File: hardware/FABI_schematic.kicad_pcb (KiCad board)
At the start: 2 copper layers, 81 x 55 mm, 74 parts, among them J1 Conn_01x02_Pin, J11 009159005551906, J11_GND1 Conn_01x01_Male, J11_VDD1 Conn_01x01_Male, J11_data1 Conn_01x01_Male, J12 Conn_01x04_Socket, J2 display_connector_91601-304LF, J3 54601-906WPLF, J4 54-00174 / FC68125, J5 54-00174 / FC68125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

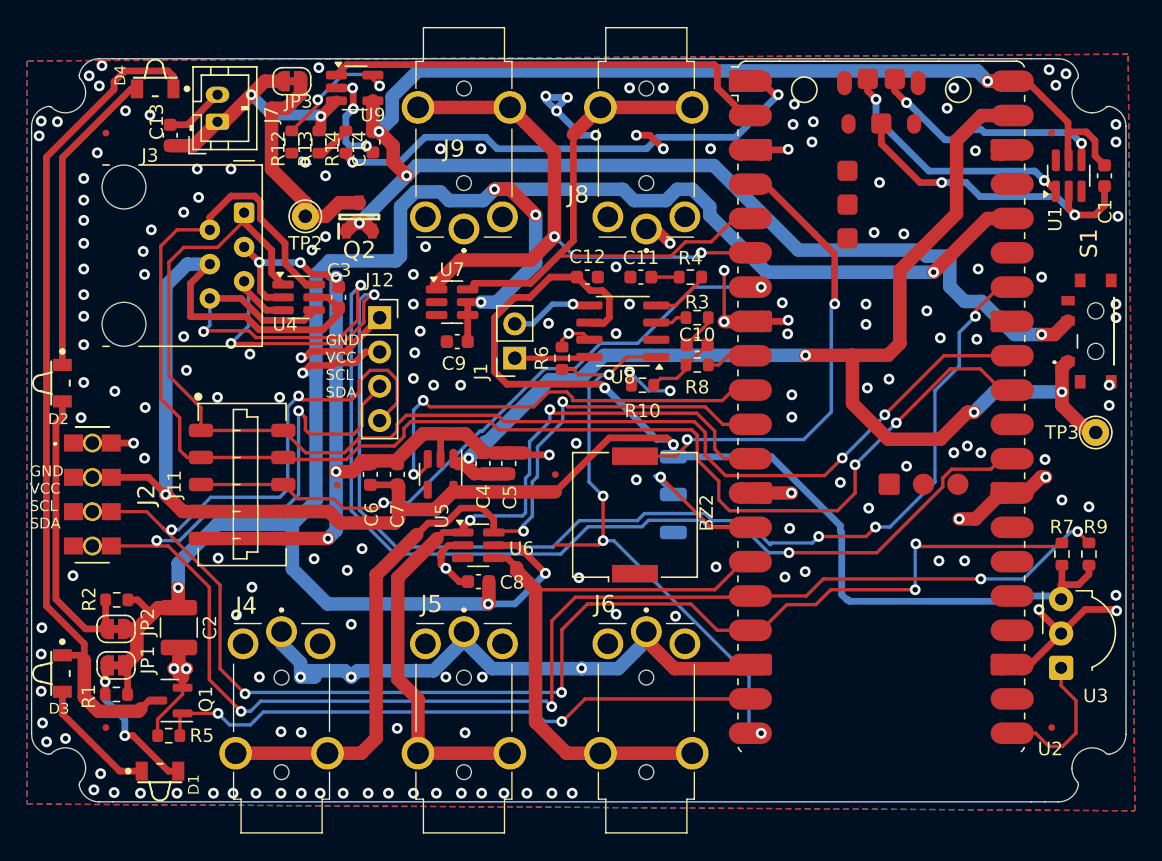
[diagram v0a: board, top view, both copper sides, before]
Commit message: Changed pins for J3 connector as it's sufficient to have I2C1 (GP18, GP19) for SDA/SCL, does not need ADC; V_BATT_MEASURE now uses GP28 with the built-in ADC; Connector J12 now uses 3.3V as well (from VCC); Improved layout;
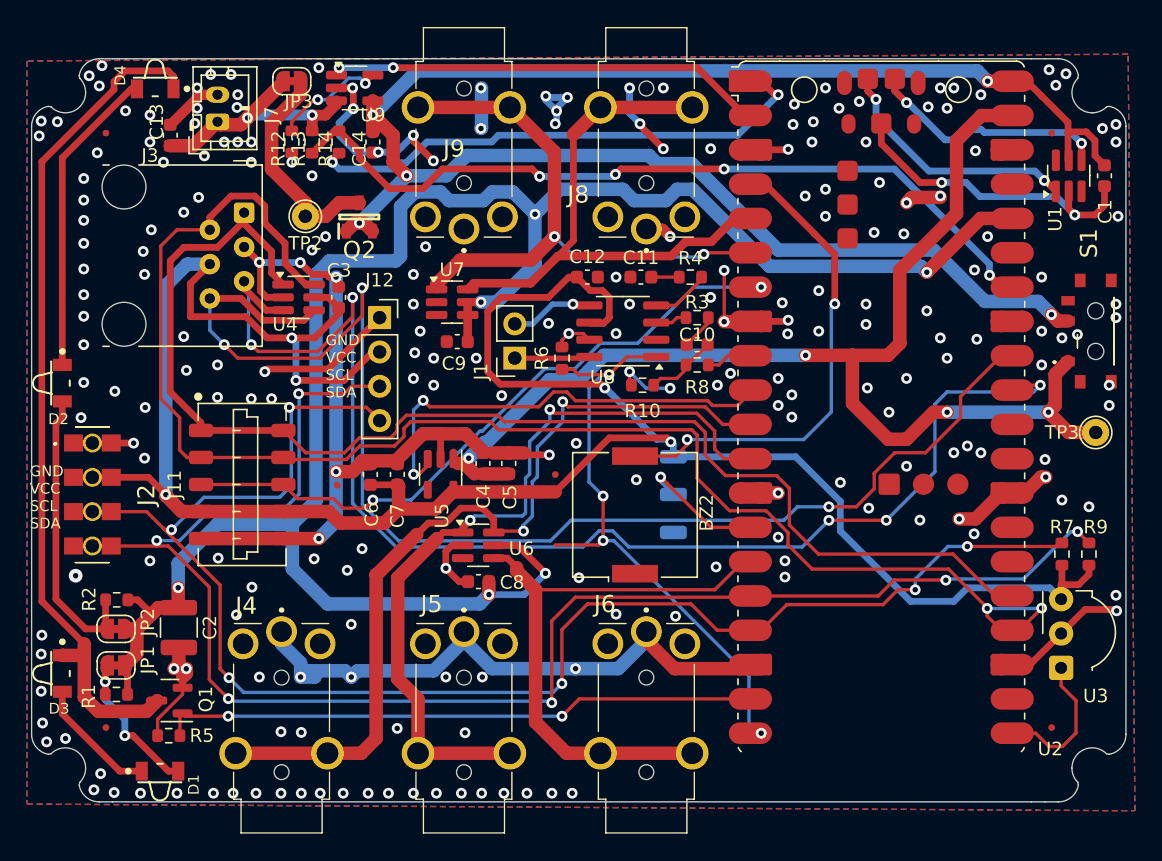
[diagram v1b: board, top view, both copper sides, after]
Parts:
- moved R13 0.50 mm to (108.0, 90.0)
- moved R14 0.50 mm to (110.0, 90.0)
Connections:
- net CHARGE_STAT renamed /CHARGE_STAT
- net V_BATT_VD_SWITCH renamed /V_BATT_VD_SWITCH
- J12 pad 2: VCC -> +3.3VADC
- R13 pad 2: V_BATT_MEASURE -> /V_BATT_MEASURE
- R14 pad 1: V_BATT_MEASURE -> /V_BATT_MEASURE
- U2 pad 24: unconnected-(U2-GPIO18-Pad24) -> /SDA
- U2 pad 25: unconnected-(U2-GPIO19-Pad25) -> /SCL
- U2 pad 29: /EXT2 -> unconnected-(U2-GPIO22-Pad29)
- U2 pad 31: /SDA -> /EXT1
- U2 pad 32: /SCL -> /EXT2
- U2 pad 34: /EXT1 -> /V_BATT_MEASURE
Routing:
- net /V_BATT_MEASURE: track 0.00 -> 59.0 mm, vias 0 -> 4
- net GND: track 199.5 -> 210.6 mm, vias 189 -> 233
- net VCC: track 159.9 -> 149.1 mm, vias 8 -> 6
- net +3.3VADC: track 167.2 -> 177.4 mm, vias 3 -> 5
- net /SCL_INT: track 125.5 -> 116.6 mm
- net /SDA: track 106.9 -> 112.9 mm
- net /EXT1: track 103.4 -> 98.2 mm
- net /SDA_INT: track 123.7 -> 120.6 mm
- net V_BATT_MEASURE: track 2.68 -> 0.00 mm
- net /SCL: track 95.3 -> 96.8 mm, vias 2 -> 0
- net Net-(U9-PROG): track 9.81 -> 8.46 mm
- net /V_BATT_VD_SWITCH: track 36.8 -> 38.0 mm
- net /IR_LED: track 46.3 -> 45.2 mm
- net /CHARGE_STAT: track 34.2 -> 33.3 mm, vias 0 -> 2
- net Net-(D3-K): track 62.5 -> 63.3 mm
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
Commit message: Removed PWR_FLAGS except for VSYS; Removed NT2 (obsolete); Updated Schematics PDF; Reduced V_PWR_SWITCH routes to 1 from 2 to make space for VCC due to it being routed around the mounting holes of connectors J8/9; Improved silkscreen; TVS Diodes routes size increased; Updated BOM;
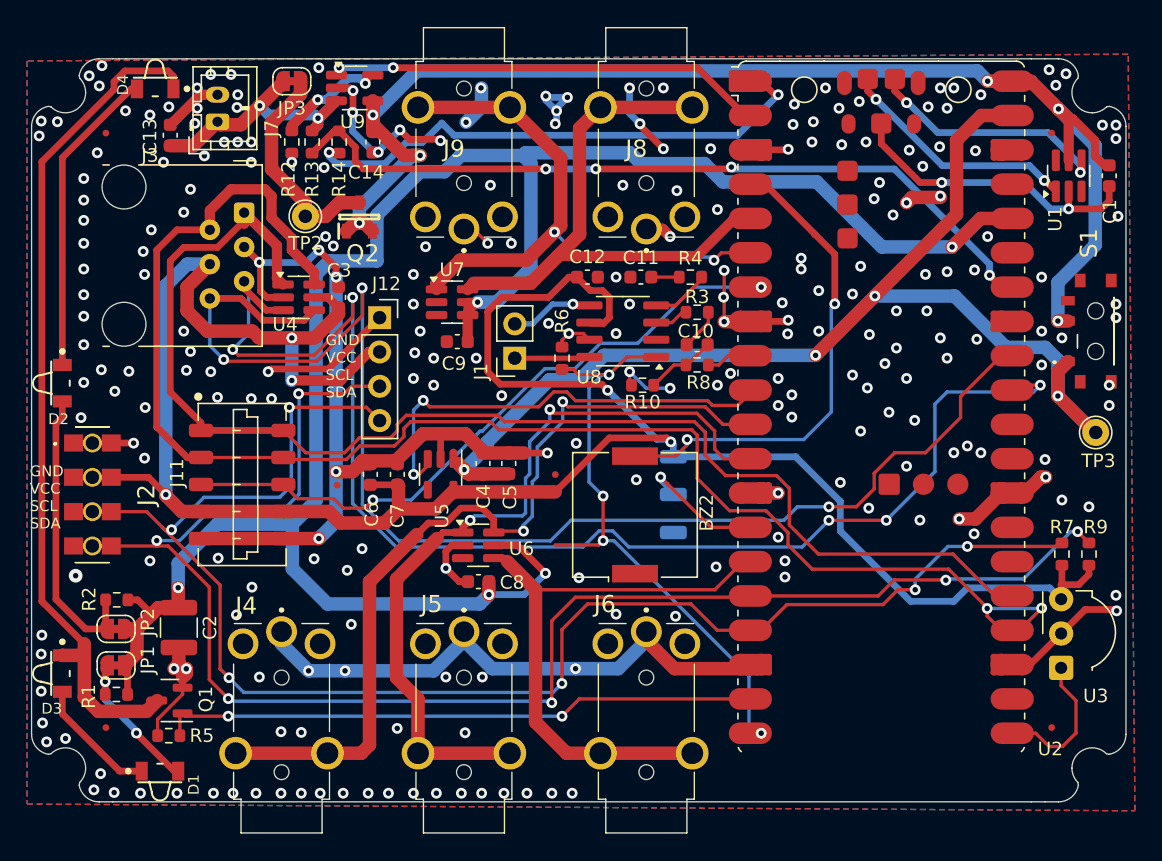
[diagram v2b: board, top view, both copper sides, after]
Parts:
- removed NT2: NetTie_2, NetTie:NetTie-2_SMD_Pad0.5mm
- moved R3 0.40 mm to (136.5, 102.6)
- moved C1 0.35 mm to (167.0, 92.5)
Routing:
- net V_PWR_SWITCH: track 132.7 -> 99.2 mm, vias 5 -> 6
- net VSYS: track 89.8 -> 84.1 mm
- net VCC: track 149.1 -> 152.7 mm, vias 6 -> 5
- net /BUTTON4: track 45.9 -> 43.0 mm
- net /EXT1: track 98.2 -> 100.4 mm
- net /SDA: track 112.9 -> 114.3 mm
- net /V_BATT_MEASURE: track 59.0 -> 57.7 mm
- net /V_BATT_VD_SWITCH: track 38.0 -> 39.1 mm
- net Net-(U1-GND): track 23.9 -> 23.0 mm
- net /EXT2: track 98.3 -> 99.1 mm
- net /SCL: track 96.8 -> 97.6 mm
- net Net-(U1-I/O1): track 18.7 -> 17.9 mm
- net V_BATT: track 19.0 -> 18.3 mm
- net GND: track 210.6 -> 211.3 mm, vias 233 -> 253
- net Net-(D1-A): track 11.9 -> 11.2 mm
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
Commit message: Moved FABI Logo; Changed some names; Changed VSYS label on LPW1; Updated SCH PDF;
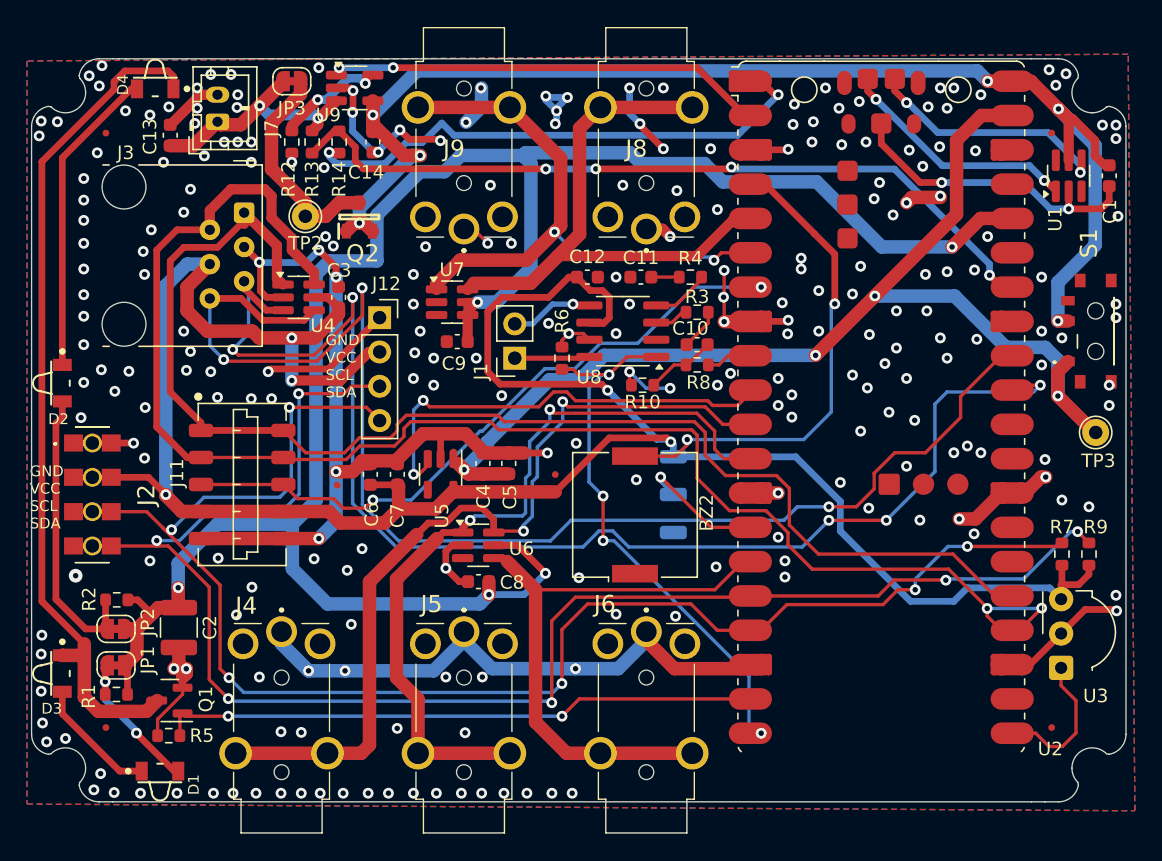
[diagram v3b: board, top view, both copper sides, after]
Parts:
- moved LOGO1 4.32 mm to (99.7, 89.6)
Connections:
- net VSYS renamed V_IN
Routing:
- net /Audio_SD: track 45.1 -> 41.4 mm
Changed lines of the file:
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@@
 	(net 64 "unconnected-(U2-SWCLK-PadD1)")
 	(net 65 "unconnected-(U8-NC-Pad2)")
-	(net 66 "VSYS")
+	(net 66 "V_IN")
 	(net 67 "Net-(C10-Pad1)")
 	(net 68 "V_BATT")
@@
 		(fp_arc
 			(start 10.579676 25.189937)
-			(mid 10.494812 25.356783)
+			(mid 10.494803 25.356771)
 			(end 10.363318 25.49)
 			(stroke
@@
 			(layers "F.Cu" "F.Paste" "F.Mask")
 			(roundrect_rratio 0.5)
-			(net 66 "VSYS")
+			(net 66 "V_IN")
 			(pinfunction "VSYS")
 			(pintype "power_in")
@@
 			(layers "*.Cu" "*.Mask")
 			(remove_unused_layers no)
-			(net 66 "VSYS")
+			(net 66 "V_IN")
 			(pinfunction "1")
 			(pintype "passive")
@@
 			(size 0.7 1)
 			(layers "F.Cu" "F.Paste" "F.Mask")
-			(net 66 "VSYS")
+			(net 66 "V_IN")
 			(pinfunction "1")
 			(pintype "passive")
@@
 			(layers "F.Cu" "F.Paste" "F.Mask")
 			(roundrect_rratio 0.25)
-			(net 66 "VSYS")
+			(net 66 "V_IN")
 			(pintype "passive")
 		)
@@
 		(tags "capacitor")
 		(property "Reference" "C10"
-			(at 0.1 1 0)
+			(at 0.5 1.2 0)
 			(layer "F.SilkS")
 			(effects
@@
 			(layers "F.Cu" "F.Paste" "F.Mask")
 			(roundrect_rratio 0.25)
-			(net 66 "VSYS")
+			(net 66 "V_IN")
 			(pinfunction "VIN")
 			(pintype "power_in")
@@
 			(layers "F.Cu" "F.Paste" "F.Mask")
 			(roundrect_rratio 0.25)
-			(net 66 "VSYS")
+			(net 66 "V_IN")
 			(pintype "passive")
 		)
@@
 		(tags "SOT-23-5 hand-soldering")
 		(property "Reference" "U9"
-			(at -0.15 2.5 180)
+			(at -1.95 2 180)
 			(layer "F.SilkS")
 			(effects
@@
 		(tags "RJ12 connector")
 		(property "Reference" "J3"
-			(at -4.23 6.97 0)
+			(at -4.43 8.77 0)
 			(layer "F.SilkS")
 			(effects
@@
 		(tags "SC-74 SO")
 		(property "Reference" "U4"
-			(at -1 2 0)
+			(at 1.8 2.1 0)
 			(layer "F.SilkS")
 			(effects
@@
 	(footprint "FABI:FABI_Logo_s"
 		(layer "B.Cu")
-		(at 104.040099 89.128395 180)
+		(at 99.740099 89.578395 180)
 		(property "Reference" "LOGO1"
 			(at 0 0 0)
@@
 	)
 	(segment
-		(start 129.54 119.507)
-		(end 129.223 119.824)
-		(width 0.25)
-		(layer "F.Cu")
-		(net 62)
-	)
-	(segment
 		(start 133.475 105.905)
 		(end 131.300743 105.905)
@@
 		(width 0.25)
 		(layer "F.Cu")
-		(net 62)
-	)
-	(segment
-		(start 129.223 119.824)
-		(end 125.984 119.824)
-		(width 0.25)
-		(layer "F.Cu")

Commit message: Changed some labels and added minor details
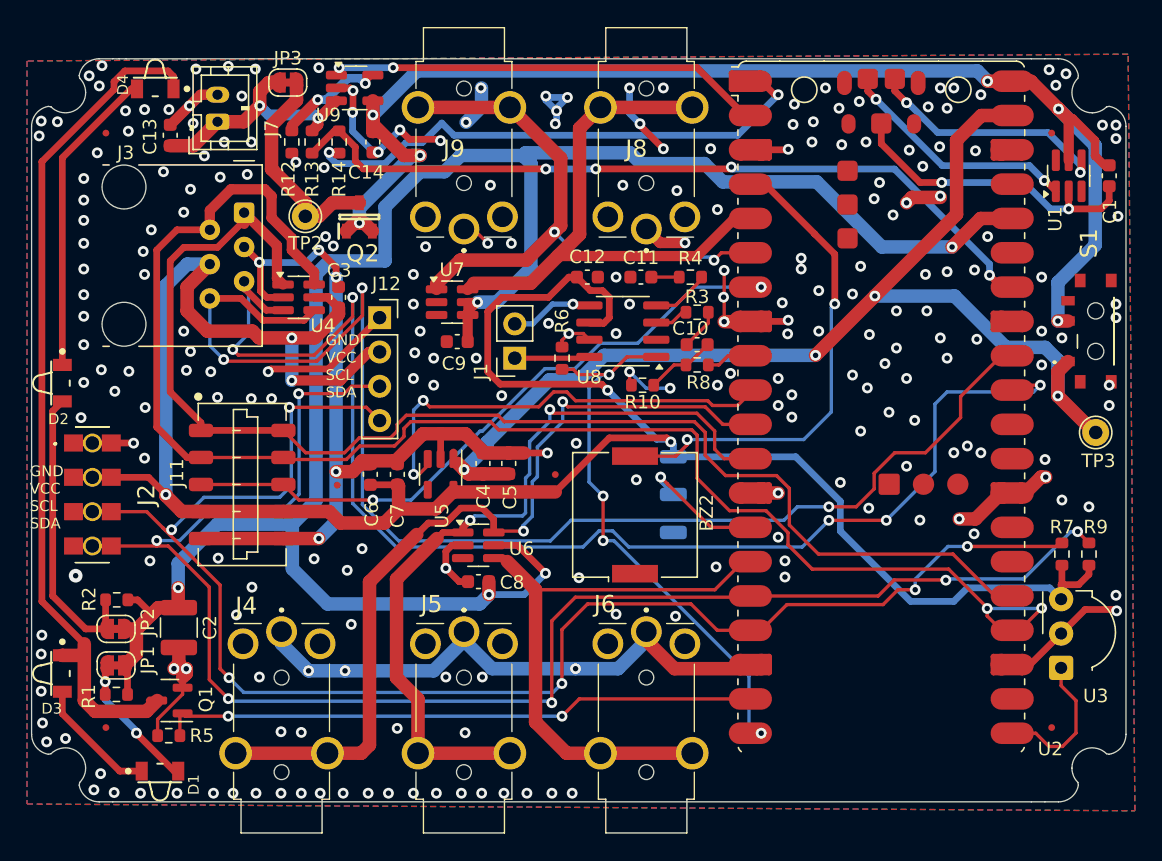
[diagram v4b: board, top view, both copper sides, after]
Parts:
- moved JP3 0.32 mm to (106.2, 85.6), turned to 0 degrees
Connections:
- JP3 pad 1: Net-(JP3-A) -> V_BATT
- JP3 pad 2: V_BATT -> Net-(JP3-B)
- Q2 pad 3: Net-(JP3-A) -> Net-(JP3-B)
- TP2 pad 1: Net-(JP3-A) -> Net-(JP3-B)
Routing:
- net Net-(JP3-A): track 16.3 -> 0.00 mm
- net Net-(JP3-B): track 0.00 -> 16.1 mm
- net GND: track 211.3 -> 212.6 mm
- net V_BATT: track 18.3 -> 18.8 mm

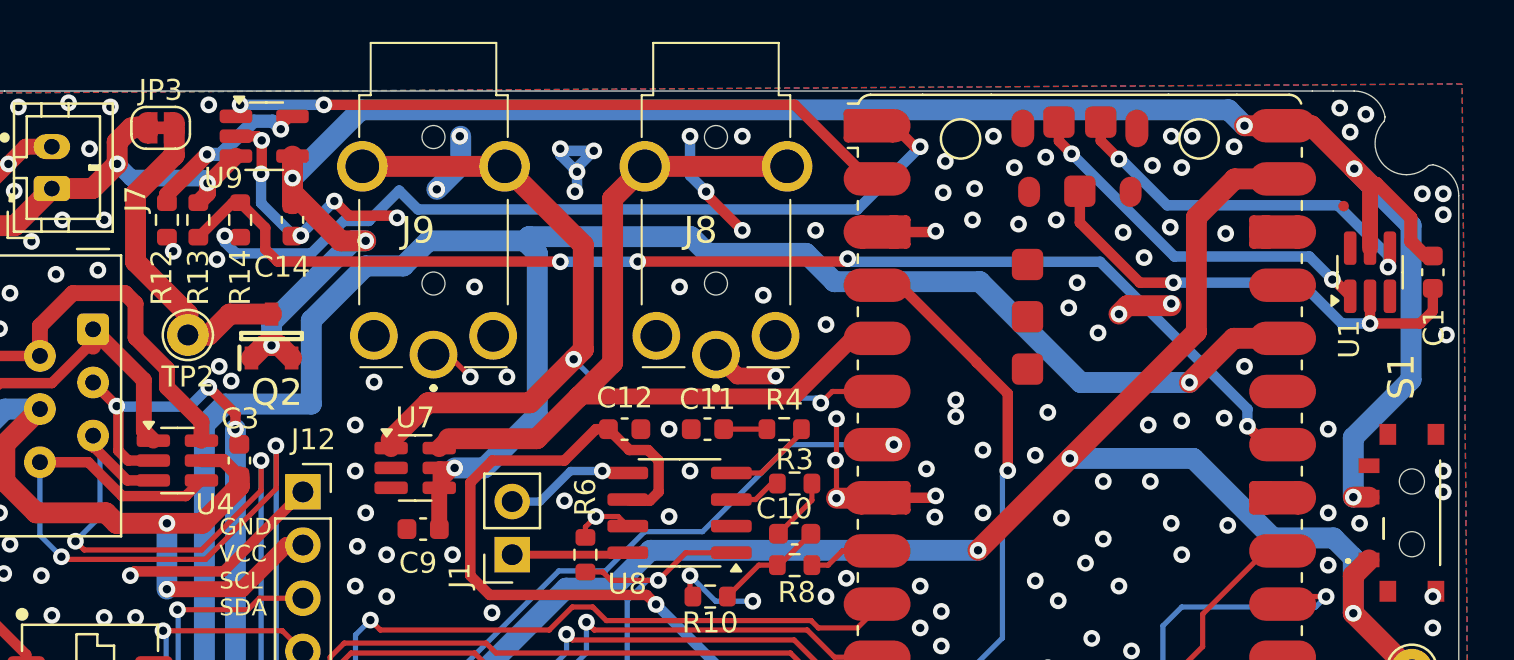
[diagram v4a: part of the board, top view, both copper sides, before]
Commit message: removed short between Mosfet G/S, some other minor changes
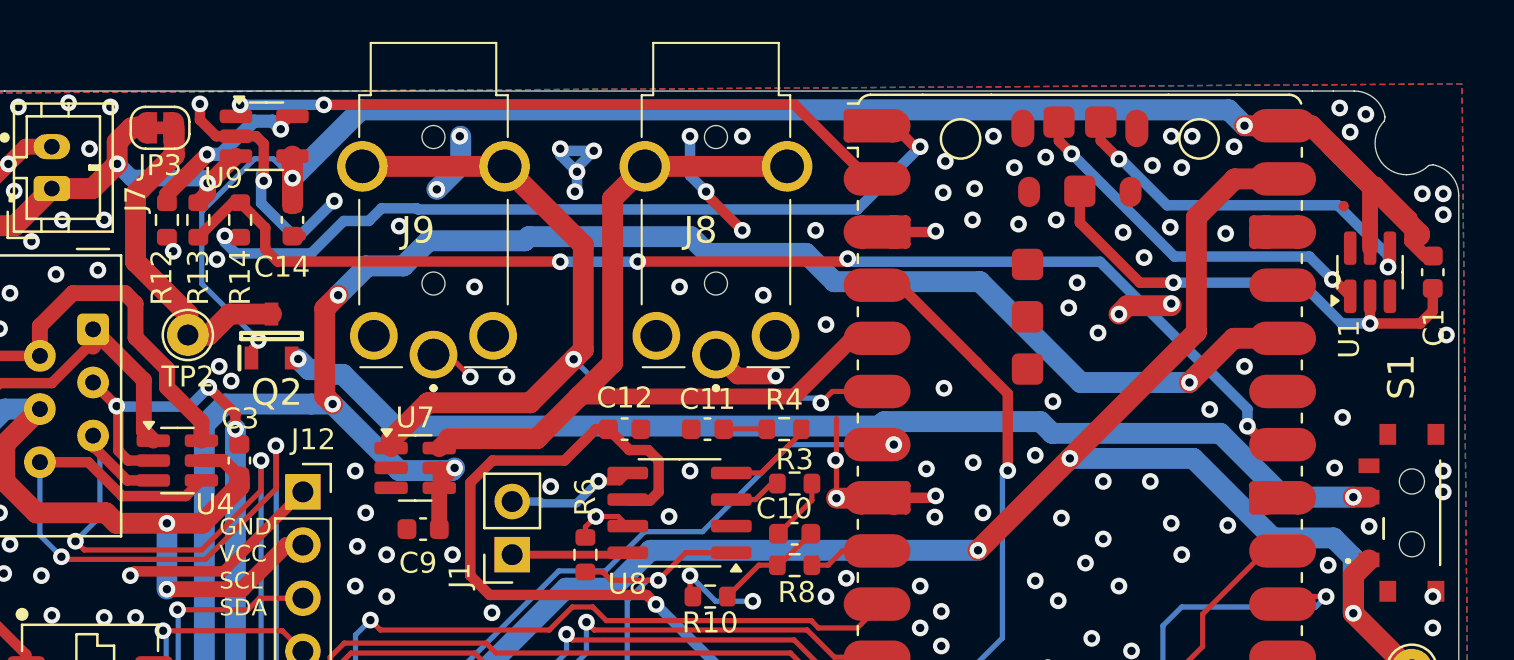
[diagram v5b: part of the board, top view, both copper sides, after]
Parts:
- turned JP3 to 180 degrees
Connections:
- net V_IN renamed VSYS
- C1 pad 1: V_PWR_SWITCH -> VBUS
- C14 pad 1: V_PWR_SWITCH -> VBUS
- JP3 pad 1: V_BATT -> Net-(JP3-A)
- JP3 pad 2: Net-(JP3-B) -> V_BATT
- Q2 pad 1: V_PWR_SWITCH -> VBUS
- Q2 pad 3: Net-(JP3-B) -> Net-(JP3-A)
- TP2 pad 1: Net-(JP3-B) -> Net-(JP3-A)
- U1 pad 5: V_PWR_SWITCH -> VBUS
- U2 pad 40: V_PWR_SWITCH -> VBUS
- U9 pad 4: V_PWR_SWITCH -> VBUS
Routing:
- net VBUS: track 0.00 -> 86.4 mm, vias 0 -> 3
- net V_PWR_SWITCH: track 99.2 -> 54.4 mm, vias 6 -> 2
- net Net-(JP3-B): track 16.1 -> 0.00 mm
- net Net-(JP3-A): track 0.00 -> 16.1 mm
- net VCC: track 153.0 -> 147.6 mm, vias 5 -> 7
- net /V_BATT_VD_SWITCH: track 39.1 -> 38.4 mm
- net GND: track 212.6 -> 212.4 mm, vias 253 -> 244
